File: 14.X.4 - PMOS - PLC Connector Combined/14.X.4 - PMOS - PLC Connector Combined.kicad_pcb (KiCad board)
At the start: 2 copper layers, 61.5 x 67.8 mm, 106 parts, among them J201 Conn_01x01_PAD, J202 Conn_01x01_PAD, J203 Conn_01x01_PAD, J204 Conn_01x01_PAD, J205 Conn_01x01_PAD, J206 Conn_01x01_PAD, J207 Conn_01x01_PAD, J208 Conn_01x01_PAD, J209 Conn_01x01_PAD, J210 Conn_01x01_PAD, J211 Conn_01x01_PAD, J212 Conn_01x01_PAD, J213 Conn_01x01_PAD, J214 Conn_01x01_PAD, J215 Conn_01x01_PAD, J216 Conn_01x01_PAD, J217 Conn_01x01_PAD, J218 Conn_01x01_PAD, J219 Conn_01x01_PAD, J220 Conn_01x01_PAD, J221 Dorabo-DB128L_5_08_2P_BKS, J222 Dorabo-DB128L_5_08_2P_BKS, J223 Dorabo-DB128L_5_08_2P_BKS, J224 Dorabo-DB128L_5_08_2P_BKS, J225 Dorabo-DB128L_5_08_2P_BKS, J226 B04B-XASK-1, J301 Conn_01x01_PAD, J302 Conn_01x01_PAD, J303 Conn_01x01_PAD, J304 Conn_01x01_PAD, J305 Conn_01x01_PAD, J306 Conn_01x01_PAD, J307 Conn_01x01_PAD, J308 Conn_01x01_PAD, J309 Conn_01x01_PAD, J310 Conn_01x01_PAD, J311 Conn_01x01_PAD, J312 Conn_01x01_PAD, J313 Conn_01x01_PAD, J314 Conn_01x01_PAD, J315 Conn_01x01_PAD, J316 Conn_01x01_PAD, J317 DB128L-5.08-2P-BK-S, J318 DB128L-5.08-3P-BK-S, J319 DB128L-5.08-2P-BK-S, J320 DB128L-5.08-2P-BK-S, J321 B04B-XASK-1, Q1 2N7002, Q2 2N7002, Q3 2N7002, Q4 2N7002, U1 DMP6023LE-13, U2 DMP6023LE-13, U3 DMP6023LE-13, U4 DMP6023LE-13

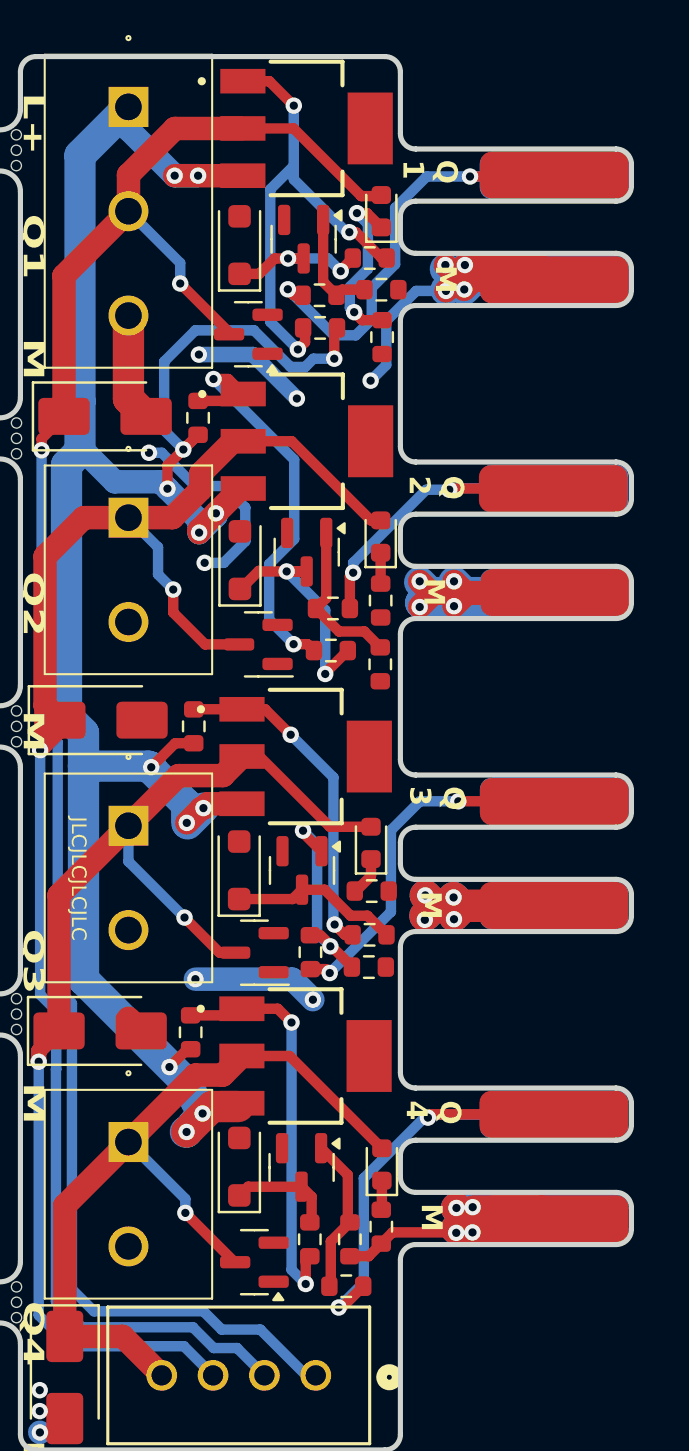
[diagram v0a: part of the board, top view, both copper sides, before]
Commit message: orientation of U1,U2,U3 and U4
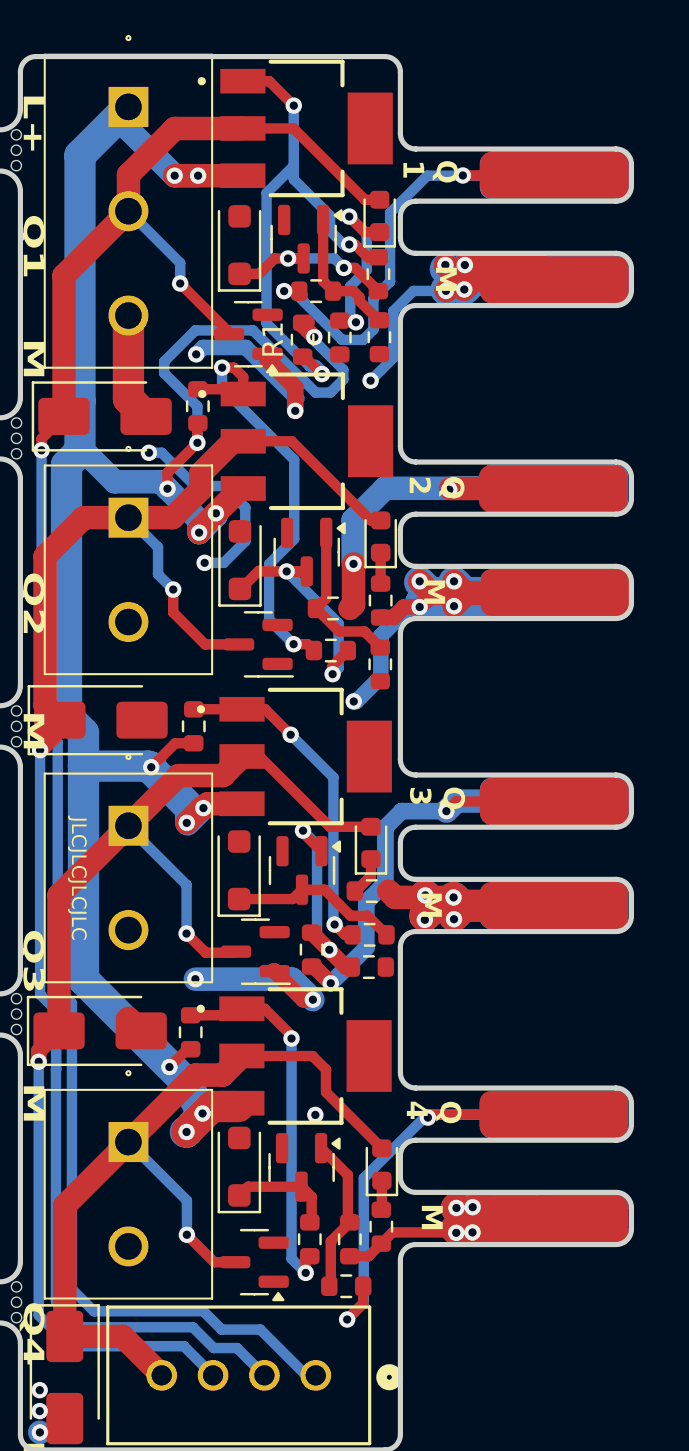
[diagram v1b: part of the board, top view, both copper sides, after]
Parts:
- J221, J222, J223, J224, J225: value Dorabo-DB128L_5_08_2P_BKS -> DB128L-5.08-2P-BK-S
- J317: value DB128L-5.08-2P-BK-S -> DB128L-5.08-2P-BK-S
- moved R2 2.32 mm to (119.7, 80.2), turned to 90 degrees
- moved R9 2.06 mm to (117.8, 80.2)
- moved R1 1.03 mm to (116.0, 80.3), turned to 90 degrees
- moved R17 0.89 mm to (119.7, 77.1), turned to 90 degrees
- moved R3 0.57 mm to (110.9, 83.6)
- moved R4 0.26 mm to (116.6, 78.0)
- moved D1 0.24 mm to (119.7, 74.3)
- moved R5 0.14 mm to (116.4, 110.0)
- moved D306 0.07 mm to (113.7, 110.1)
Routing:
- net GNDPWR: track 225.6 -> 243.7 mm, vias 26 -> 28
- net Net-(J314-Pin_1): track 17.7 -> 24.2 mm
- net Net-(J306-Pin_1): track 18.7 -> 25.0 mm
- net Net-(J318-Pad1): track 115.6 -> 118.3 mm
- net Net-(R1-Pad1): track 24.1 -> 26.6 mm
- net Net-(R19-Pad1): track 19.8 -> 18.4 mm
- net Net-(D3-A): track 40.2 -> 41.4 mm
- net Net-(Q4-G): track 5.41 -> 6.62 mm
- net Net-(D5-K): track 7.16 -> 8.33 mm
- net Net-(J304-Pin_1): track 24.8 -> 25.8 mm
- net Net-(J302-Pin_1): track 25.2 -> 25.9 mm
- net Net-(D1-K): track 7.96 -> 8.56 mm
- net Net-(Q2-G): track 9.80 -> 10.4 mm
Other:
- board text added: "14.1.1"
- board text removed: "12.1.1"
